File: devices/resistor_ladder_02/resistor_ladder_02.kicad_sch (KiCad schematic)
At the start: 8 parts

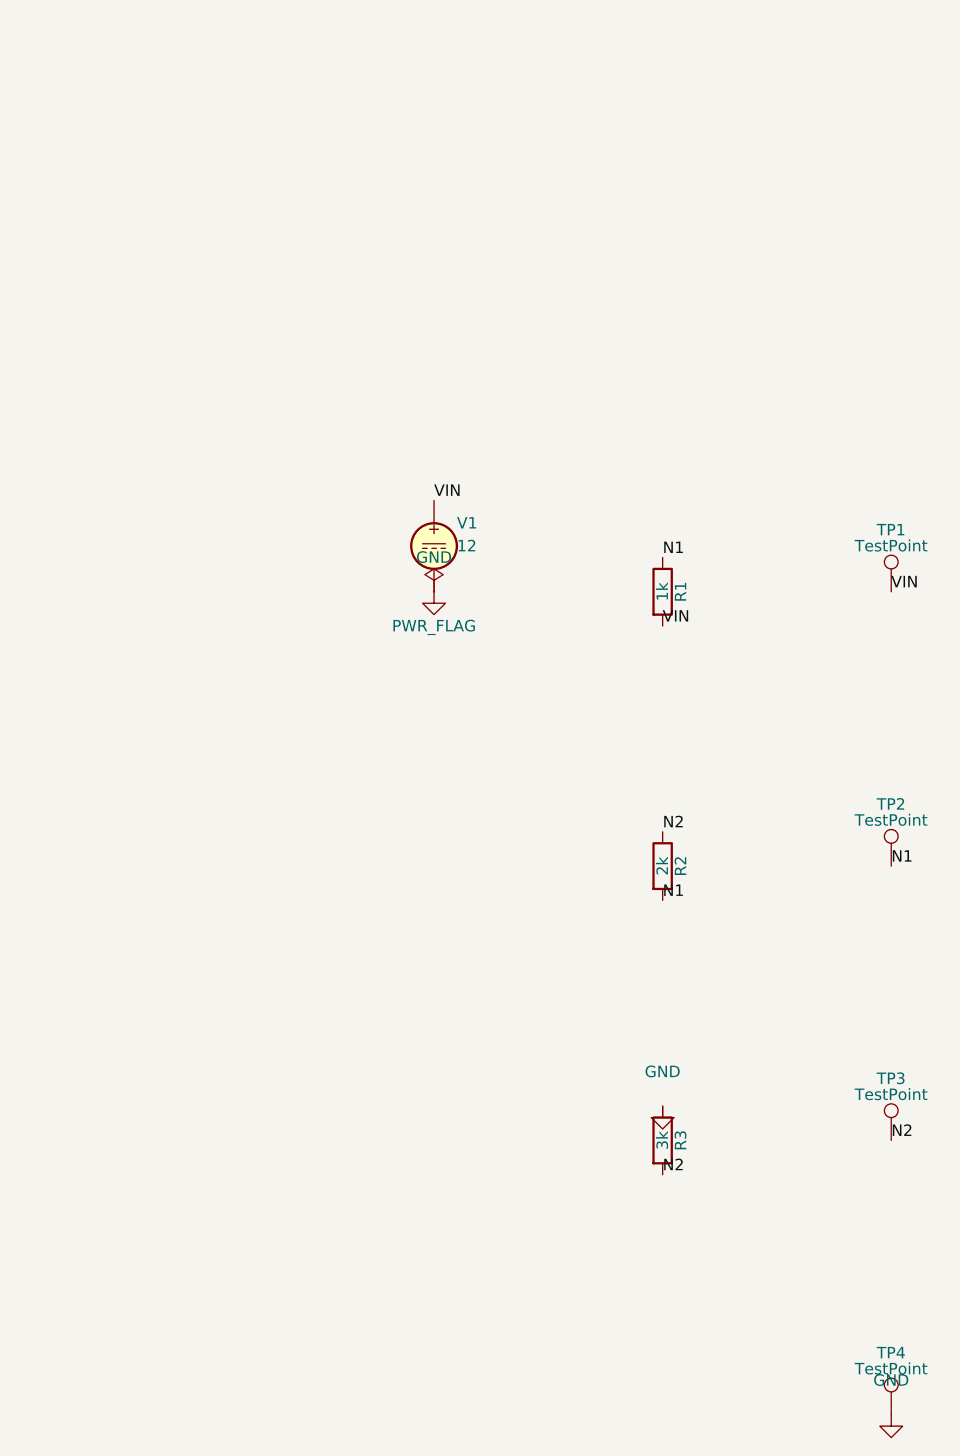
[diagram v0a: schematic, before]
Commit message: Schematics: draw real wires between components, not just net labels
Confirmed the diagnosis before touching anything: every device's .kicad_sch
had zero (wire ...) elements -- connectivity was entirely via same-named
net labels (which KiCad does merge into one net sheet-wide with no wire
between them, confirmed empirically). Correct for simulation/netlist
purposes, but the schematic view rendered as scattered disconnected
symbols with floating TP markers -- not because of a KiCanvas rendering
gap, but because there was genuinely no wire geometry in the source.

Rebuilds all 5 devices with real (wire ...) segments and (junction ...)
dots connecting every pin, and repositions each TP marker to tap directly
off its wire instead of floating in its own column. Also switches every
device from a full A4 sheet to a compact page sized to its own circuit
(kicadCoords.ts's schematicMmToPixels updated to match) -- on A4 the
actual symbols were tiny relative to the fixed-size TP marker overlay;
sized to content, the same symbols occupy far more of the viewport.

Two real routing bugs found and fixed via ERC + a real exported netlist
at every step (not just "0 ERC errors", which doesn't catch either of
these):
- diode_indicator_03: two different nets' horizontal wire runs shared the
  same Y with overlapping X ranges -- collinear overlap merges wires into
  one net, same as overlapping copper would, silently folding GND and N1
  together.
- resistor_bridge_05: a tap wire spanned past a component's *other* pin
  along the same column (a pin lying anywhere along a wire's path counts
  as connected, not just at a declared endpoint) -- collapsed every net
  into one. Also separately found: two adjacent TP markers ended up only
  3.81mm apart, too close for the existing 44px mobile tap target to not
  overlap -- widened that specific gap.

Verified end-to-end after deploying: every device re-imported through the
real API, full backend+frontend suites green, and a live-browser sweep of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
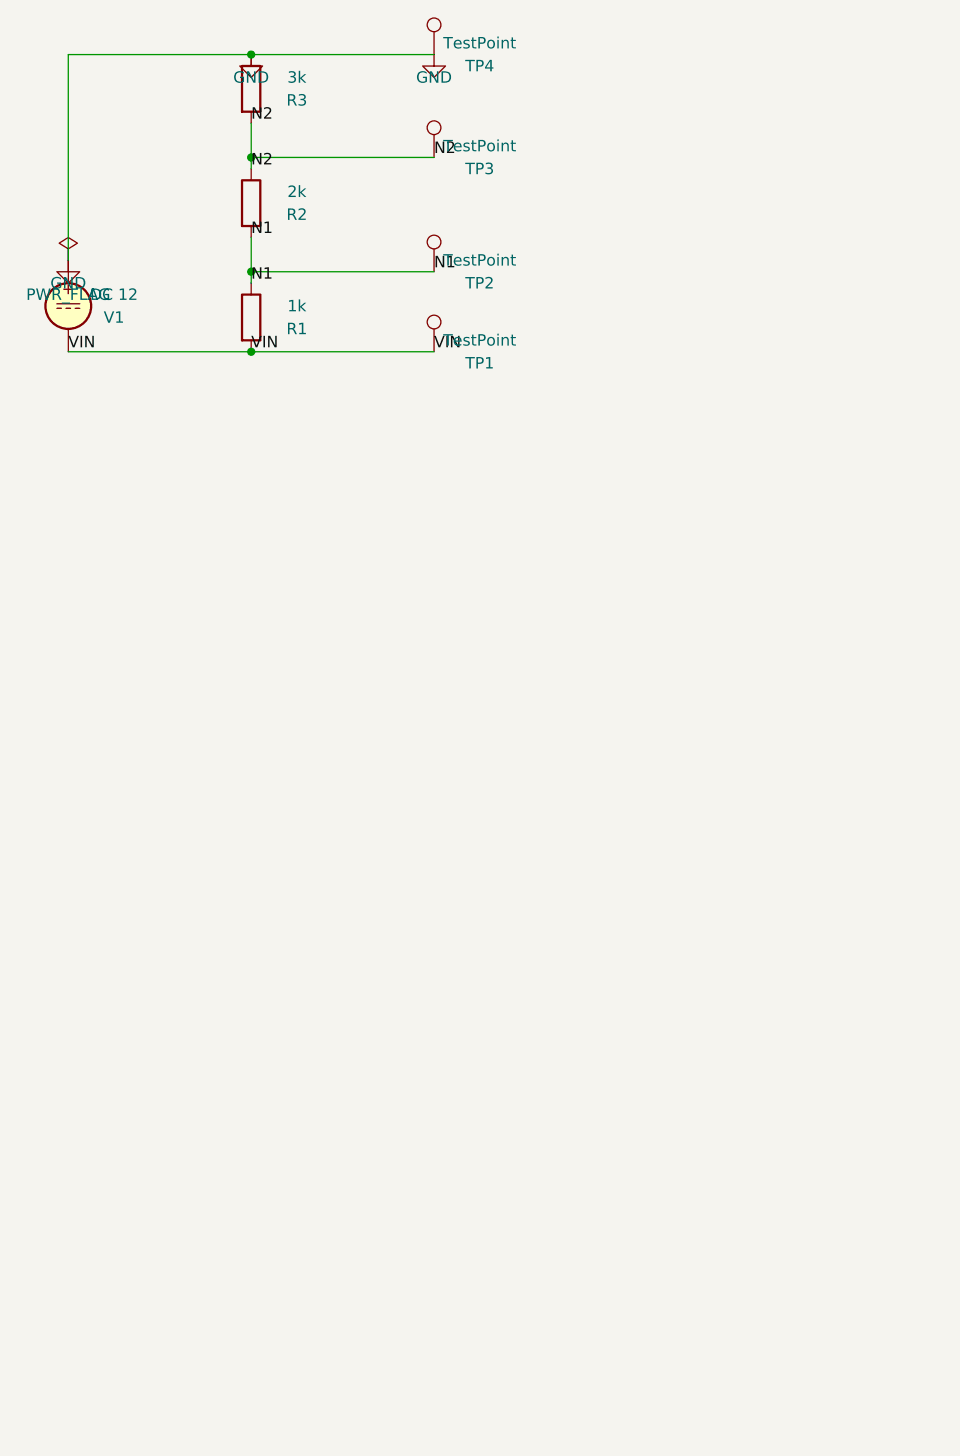
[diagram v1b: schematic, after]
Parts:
- V1: value 12 -> DC 12
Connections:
- net GND: now also V1.1; no longer V1.2
- net VIN: now also V1.2; no longer V1.1
